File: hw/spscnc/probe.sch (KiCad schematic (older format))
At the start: 14 parts, among them K5 HFD3/3, U6 IL0515S_DC-DC, U7 LBA710

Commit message: added most corrections on the schematic for i2s operation.
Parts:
- ISO_PROBE1: footprint industrial000:rj45_R-RJ45S08P-B000_C386763 -> industrial:rj45_R-RJ45S08P-B000_C386763
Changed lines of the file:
@@
 $Descr A4 11693 8268
 encoding utf-8
-Sheet 9 16
+Sheet 9 17
 Title "Trinamic FluidNC CNC Controller"
 Date "2022-01-27"
@@
 F 0 "ISO_PROBE1" H 8445 1572 50  0000 R CNN
 F 1 "8P8C_4xShielded" H 8445 1663 50  0000 R CNN
-F 2 "industrial000:rj45_R-RJ45S08P-B000_C386763" V 8775 1675 50  0001 C CNN
+F 2 "industrial:rj45_R-RJ45S08P-B000_C386763" V 8775 1675 50  0001 C CNN
 F 3 "~" V 8775 1675 50  0001 C CNN
 F 4 "DNP007" H 8775 1650 50  0001 C CNN "jlcpcb"

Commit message: began routing of the i2so part
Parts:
- added D56: 1N4148, Diode_SMD:D_SOD-123, symbol Diode:1N4148
- added K1: HFD3/3, Relay_THT:Relay_DPDT_Kemet_EC2, symbol Relay:EC2-3NU
- added R197: 1K, Resistor_SMD:R_0603_1608Metric, symbol Device:R
- added U15: LBA710, Package_DIP:DIP-8_W8.89mm_SMDSocket_LongPads, symbol industrial:LBA710
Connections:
- net +24V: now also K1.4, K1.9
- net +3V3: now also R197.1, U15.6
- net GND: now also D56.2 (A), K1.12
- net VACUUM_EN: now also K1.10; no longer K5.10
- new net: R197.2, U15.3
- new net: D56.1 (K), K1.1, U15.5
- new net ENABLE_VACUUM: U15.4
- no-connect marks 6 -> 10
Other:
- note added: "This connector drives External 24V relays which enable the 230V circuits."
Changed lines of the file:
@@
 Wire Wire Line
 	8975 5575 8975 5375
-Text GLabel 9125 4650 2    50   Output ~ 0
-VACUUM_EN
-Wire Wire Line
-	9125 4650 8875 4650
-Wire Wire Line
-	8875 4650 8875 4775
 Text GLabel 5275 5625 2    50   Output ~ 0
 VACUUM_EN
@@
 Wire Wire Line
 	6800 4625 6875 4625
+$Comp
+L industrial:LBA710 U15
+U 2 1 620C5BE0
+P 1950 4650
+F 0 "U15" H 1950 4975 50  0000 C CNN
+F 1 "LBA710" H 1950 4884 50  0000 C CNN
+F 2 "Package_DIP:DIP-8_W8.89mm_SMDSocket_LongPads" H 1750 4450 50  0001 L CIN
+F 3 "https://toshiba.semicon-storage.com/info/docget.jsp?did=17036&prodName=TLP222A" H 1950 4650 50  0001 L CNN
+F 4 "own stock" H 1950 4650 50  0001 C CNN "alternatives"
+F 5 "DNP014" H 1950 4650 50  0001 C CNN "jlcpcb"
+	2    1950 4650
+	1    0    0    -1
+$EndComp
+Text GLabel 1575 4750 0    50   Input ~ 0
+ENABLE_VACUUM
+$Comp
+L Device:R R?
+U 1 1 620C5BEB
+P 1525 4400
+AR Path="/5AD47FD6/620C5BEB" Ref="R?"  Part="1"
+AR Path="/61FBB705/620C5BEB" Ref="R?"  Part="1"
+AR Path="/5AD46BE5/620C5BEB" Ref="R?"  Part="1"
+AR Path="/5AD46BE5/619A452E/620C5BEB" Ref="R?"  Part="1"
+AR Path="/620C5BEB" Ref="R?"  Part="1"
+AR Path="/61B9A8A6/620C5BEB" Ref="R?"  Part="1"
+AR Path="/61C743E7/61B9A8A6/620C5BEB" Ref="R?"  Part="1"
+AR Path="/61C81F9D/620C5BEB" Ref="R?"  Part="1"
+AR Path="/61DEDDC1/620C5BEB" Ref="R197"  Part="1"
+F 0 "R197" V 1605 4400 50  0000 C CNN
+F 1 "1K" V 1525 4400 50  0000 C CNN
+F 2 "Resistor_SMD:R_0603_1608Metric" V 1455 4400 50  0001 C CNN
+F 3 "" H 1525 4400 50  0001 C CNN
+F 4 "" V 1525 4400 60  0001 C CNN "farnell"
+F 5 "C21190" H 1525 4400 50  0001 C CNN "jlcpcb"
+F 6 "5%" H 1525 4400 50  0001 C CNN "precision"
+F 7 "1%" H 1525 4400 50  0001 C CNN "power"
+	1    1525 4400
+	1    0    0    -1
+$EndComp
+Wire Wire Line
+	2250 4550 2425 4550
+Wire Wire Line
+	2425 4550 2425 4450
+$Comp
+L Relay:EC2-3NU K1
+U 1 1 620C5BF4
+P 3350 5200
+F 0 "K1" H 3980 5246 50  0000 L CNN
+F 1 "HFD3/3" H 3980 5155 50  0000 L CNN
+F 2 "Relay_THT:Relay_DPDT_Kemet_EC2" H 3350 5200 50  0001 C CNN
+F 3 "https://content.kemet.com/datasheets/KEM_R7002_EC2_EE2.pdf" H 3350 5200 50  0001 C CNN
+F 4 "DNP009" H 3350 5200 50  0001 C CNN "jlcpcb"
+	1    3350 5200
+	1    0    0    -1
+$EndComp
+Wire Wire Line
+	2250 4750 2550 4750
+Wire Wire Line
+	2950 4750 2950 4900
+$Comp
+L industrial:+3V3 #PWR0270
+U 1 1 620C5BFC
+P 2425 4450
+F 0 "#PWR0270" H 2425 4300 50  0001 C CNN
+F 1 "+3V3" H 2440 4623 50  0000 C CNN
+F 2 "" H 2425 4450 50  0001 C CNN
+F 3 "" H 2425 4450 50  0001 C CNN
+	1    2425 4450
+	1    0    0    -1
+$EndComp
+$Comp
+L power:GND-power #PWR?
+U 1 1 620C5C02
+P 2950 5675
+AR Path="/620C5C02" Ref="#PWR?"  Part="1"
+AR Path="/61DEDDC1/620C5C02" Ref="#PWR0271"  Part="1"
+F 0 "#PWR0271" H 2950 5425 50  0001 C CNN
+F 1 "GND" H 2955 5502 50  0000 C CNN
+F 2 "" H 2950 5675 50  0001 C CNN
+F 3 "" H 2950 5675 50  0001 C CNN
+	1    2950 5675
+	1    0    0    -1
+$EndComp
+$Comp
+L Diode:1N4148 D56
+U 1 1 620C5C09
+P 2550 5200
+F 0 "D56" V 2500 4875 50  0000 L CNN
+F 1 "1N4148" V 2600 4825 50  0000 L CNN
+F 2 "Diode_SMD:D_SOD-123" H 2550 5025 50  0001 C CNN
+F 3 "https://assets.nexperia.com/documents/data-sheet/1N4148_1N4448.pdf" H 2550 5200 50  0001 C CNN
+F 4 "C81598" V 2550 5200 50  0001 C CNN "jlcpcb"
+	1    2550 5200
+	0    1    1    0
+$EndComp
+Wire Wire Line
+	2550 5050 2550 4750
+Connection ~ 2550 4750
+Wire Wire Line
+	2550 4750 2950 4750
+Wire Wire Line
+	2550 5350 2550 5550
+Wire Wire Line
+	2550 5550 2950 5550
+Wire Wire Line
+	2950 5550 2950 5675
+Wire Wire Line
+	2950 5550 2950 5500
+Connection ~ 2950 5550
+$Comp
+L power:+24V-power #PWR?
+U 1 1 620C5C17
+P 3950 5700
+AR Path="/620C5C17" Ref="#PWR?"  Part="1"
+AR Path="/61DEDDC1/620C5C17" Ref="#PWR0272"  Part="1"
+F 0 "#PWR0272" H 3950 5550 50  0001 C CNN
+F 1 "+24V" H 3965 5873 50  0000 C CNN
+F 2 "" H 3950 5700 50  0001 C CNN
+F 3 "" H 3950 5700 50  0001 C CNN
+	1    3950 5700
+	1    0    0    -1
+$EndComp
+Wire Wire Line
+	3350 5700 3350 5500
+NoConn ~ 3450 4900
+NoConn ~ 3850 4900
+Wire Wire Line
+	3750 5700 3750 5500
+Text GLabel 3900 4775 2    50   Output ~ 0
+VACUUM_EN
+Wire Wire Line
+	3900 4775 3650 4775
+Wire Wire Line
+	3650 4775 3650 4900
+Wire Wire Line
+	3950 5700 3750 5700
+Wire Wire Line
+	3750 5700 3350 5700
+Connection ~ 3750 5700
+$Comp
+L industrial:+3V3 #PWR0269
+U 1 1 620C5C2A
+P 1525 4250
+F 0 "#PWR0269" H 1525 4100 50  0001 C CNN
+F 1 "+3V3" H 1540 4423 50  0000 C CNN
+F 2 "" H 1525 4250 50  0001 C CNN
+F 3 "" H 1525 4250 50  0001 C CNN
+	1    1525 4250
+	1    0    0    -1
+$EndComp
+Wire Wire Line
+	1650 4550 1525 4550
+Wire Wire Line
+	1575 4750 1650 4750
+NoConn ~ 8875 4775
+NoConn ~ 3250 4900
+Text Notes 4325 6400 0    50   ~ 0
+This connector drives External 24V relays which enable the 230V circuits.
 $EndSCHEMATC

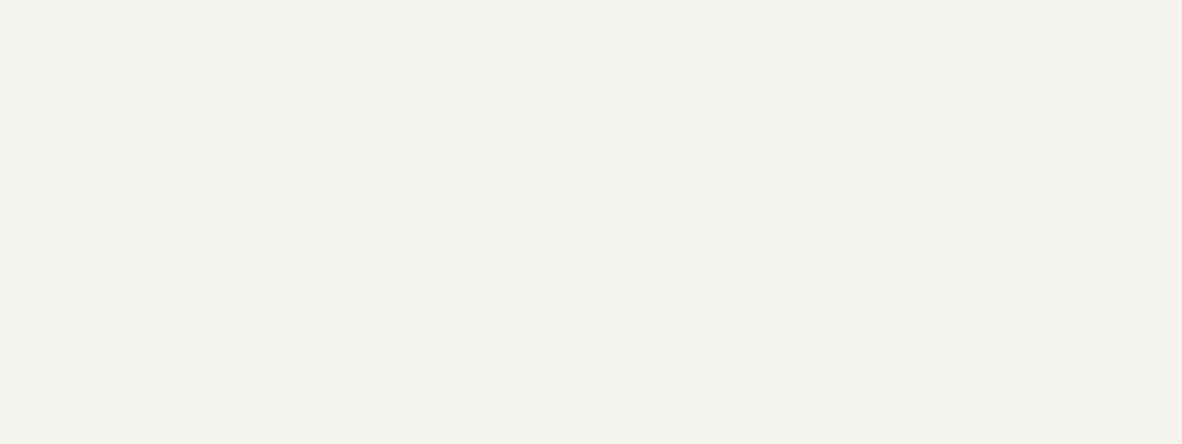
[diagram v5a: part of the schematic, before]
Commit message: Prototype corrections without new PCB
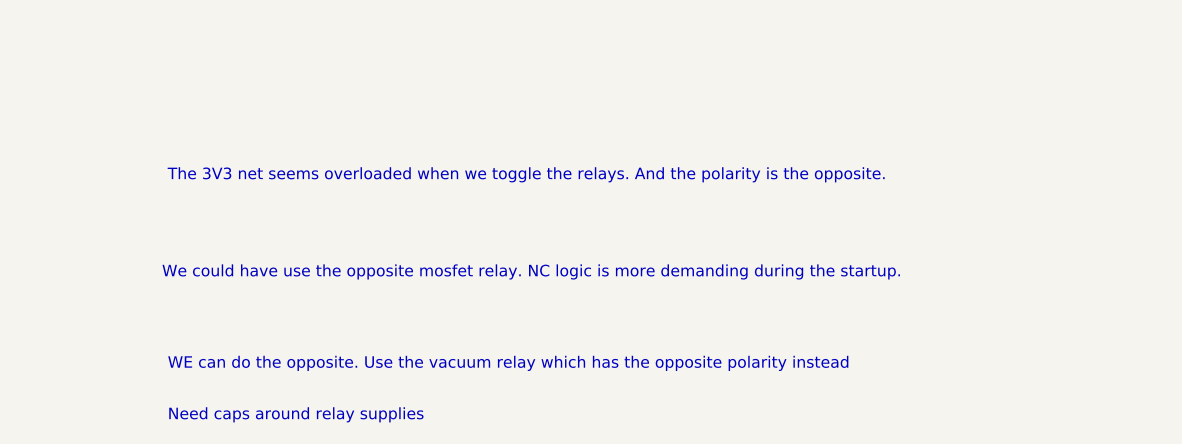
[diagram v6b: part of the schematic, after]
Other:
- note added: "Need caps around relay supplies"
- note added: "The 3V3 net seems overloaded when we toggle the relays. And the polarity is the opposite.\n"
- note added: "WE can do the opposite. Use the vacuum relay which has the opposite polarity instead\n"
- note added: "We could have use the opposite mosfet relay. NC logic is more demanding during the startup."
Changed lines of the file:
@@
 Text Notes 4325 6400 0    50   ~ 0
 This connector drives External 24V relays which enable the 230V circuits.
+Text Notes 5925 8925 0    50   ~ 0
+The 3V3 net seems overloaded when we toggle the relays. And the polarity is the opposite.\n
+Text Notes 5900 9350 0    50   ~ 0
+We could have use the opposite mosfet relay. NC logic is more demanding during the startup.
+Text Notes 5925 9750 0    50   ~ 0
+WE can do the opposite. Use the vacuum relay which has the opposite polarity instead\n
+Text Notes 5925 9975 0    50   ~ 0
+Need caps around relay supplies
 $EndSCHEMATC

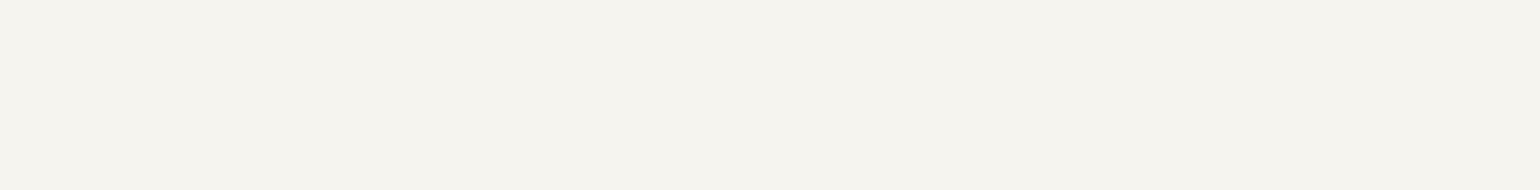
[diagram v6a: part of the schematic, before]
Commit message: Reported more defects
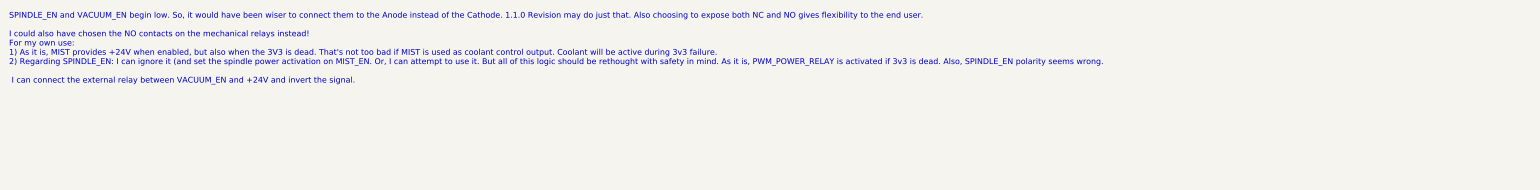
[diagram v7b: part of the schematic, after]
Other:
- note added: "SPINDLE_EN and VACUUM_EN begin low. So, it would have been wiser to connect them to the Anode instead of the Cathode. 1.1.0 Revision may do just that. Also choosing to expose both NC and NO gives flexibility to the end user.\n\nI could also have chosen the NO contacts on the mechanical relays instead!\nFor my own use:\n1) As it is, MIST provides +24V when enabled, but also when the 3V3 is dead. T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"
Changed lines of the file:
@@
 Text Notes 5925 9975 0    50   ~ 0
 Need caps around relay supplies
+Text Notes -275 -175 0    50   ~ 0
+SPINDLE_EN and VACUUM_EN begin low. So, it would have been wiser to connect them to the Anode instead of the Cathode. 1.1.0 Revision may do just that. Also choosing to expose both NC and NO gives flexibility to the end user.\n\nI could also have chosen the NO contacts on the mechanical relays instead!\nFor my own use:\n1) As it is, MIST provides +24V when enabled, but also when the 3V3 is dead. That's not too bad if MIST is used as coolant control output. Coolant will be active during 3v3 failure.\n2) Regarding SPINDLE_EN: I can ignore it (and set the spindle power activation on MIST_EN. Or, I can attempt to use it. But all of this logic should be rethought with safety in mind. As it is, PWM_POWER_RELAY is activated if 3v3 is dead. Also, SPINDLE_EN polarity seems wrong.\n\n I can connect the external relay between VACUUM_EN and +24V and invert the signal.\n\n\n
 $EndSCHEMATC
